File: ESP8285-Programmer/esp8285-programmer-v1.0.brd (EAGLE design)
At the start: 38.2 x 15.2 mm, 30 parts, among them J1 6p-2.54, J2 2p-2.54, J3 2p-2.54, K1 B3U-1000P, Q1 S9013, Q2 S9013, U1 CH340T-SSOP20, U2 CJA1117B-3.3-SOT89, Y1 12MHZ

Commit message: Another Rev 1.0
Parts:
- moved J1 40.7 mm to (2.54, 22.9), turned to 180 degrees
- moved F1 34.9 mm to (6.35, 16.5), turned to 0 degrees
- moved K1 34.8 mm to (6.29, 27.2), turned to 270 degrees
- moved R4 33.9 mm to (6.48, 19.4), turned to 270 degrees
- moved R5 33.5 mm to (6.48, 21.1), turned to 270 degrees
- moved R6 33.5 mm to (6.48, 22.9), turned to 270 degrees
- moved D1 30.7 mm to (37.0, 28.3), turned to 0 degrees
- moved R1 29.5 mm to (37.0, 26.5), turned to 90 degrees
- moved D4 29.2 mm to (9.59, 28.3), turned to 180 degrees
- moved R9 27.9 mm to (9.59, 26.5), turned to 270 degrees
- moved J3 25.7 mm to (11.3, 16.5), turned to 270 degrees
- moved USB 23.2 mm to (34.3, 20.3), turned to 90 degrees
- moved D2 22.9 mm to (13.1, 28.3), turned to 180 degrees
- moved Q2 22.8 mm to (11.5, 23.4), turned to 0 degrees
- moved R3 21.4 mm to (12.7, 18.9), turned to 90 degrees
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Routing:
- net N$15: track 2.64 -> 3.34 mm
- net N$14: track 2.59 -> 3.29 mm
- net N$RX: track 15.8 -> 15.1 mm
- net +3V3: track 63.0 -> 62.3 mm
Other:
- board text added: "Io0"
- board text added: "Rx"

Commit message: Hopefully final V1.0
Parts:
- moved D1 43.3 mm to (2.41, 2.16), turned to 180 degrees
- moved R1 41.2 mm to (2.41, 4.00), turned to 270 degrees
- moved J1 37.5 mm to (36.8, 7.62), turned to 0 degrees
- moved K1 35.9 mm to (33.1, 3.30), turned to 90 degrees
- moved U2 34.7 mm to (7.37, 3.05), turned to 180 degrees
- moved D4 33.0 mm to (29.8, 2.16), turned to 0 degrees
- moved USB 30.9 mm to (5.08, 10.2), turned to 270 degrees
- moved R6 30.5 mm to (32.9, 7.62), turned to 90 degrees
- moved R9 30.2 mm to (29.8, 4.00), turned to 90 degrees
- moved D2 29.3 mm to (26.2, 2.16), turned to 0 degrees
- moved C4 29.1 mm to (7.24, 7.68), turned to 0 degrees
- moved R4 28.3 mm to (32.9, 9.33), turned to 90 degrees
- moved R5 28.3 mm to (32.9, 11.0), turned to 90 degrees
- moved D3 26.8 mm to (22.7, 2.16), turned to 0 degrees
- moved F1 26.8 mm to (33.0, 14.0), turned to 180 degrees
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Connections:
- removed net N$14: J1.2, R4.2
- removed net N$15: J1.3, R5.2
- new net N$4: J1.2, R5.2
- new net N$7: J1.3, R4.2
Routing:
- net N$7: track 0.00 -> 3.36 mm
- net N$15: track 3.34 -> 0.00 mm
- net N$4: track 0.00 -> 3.33 mm
- net N$14: track 3.29 -> 0.00 mm
- net N$TX: track 17.9 -> 15.6 mm
- net N$RX: track 15.1 -> 15.8 mm

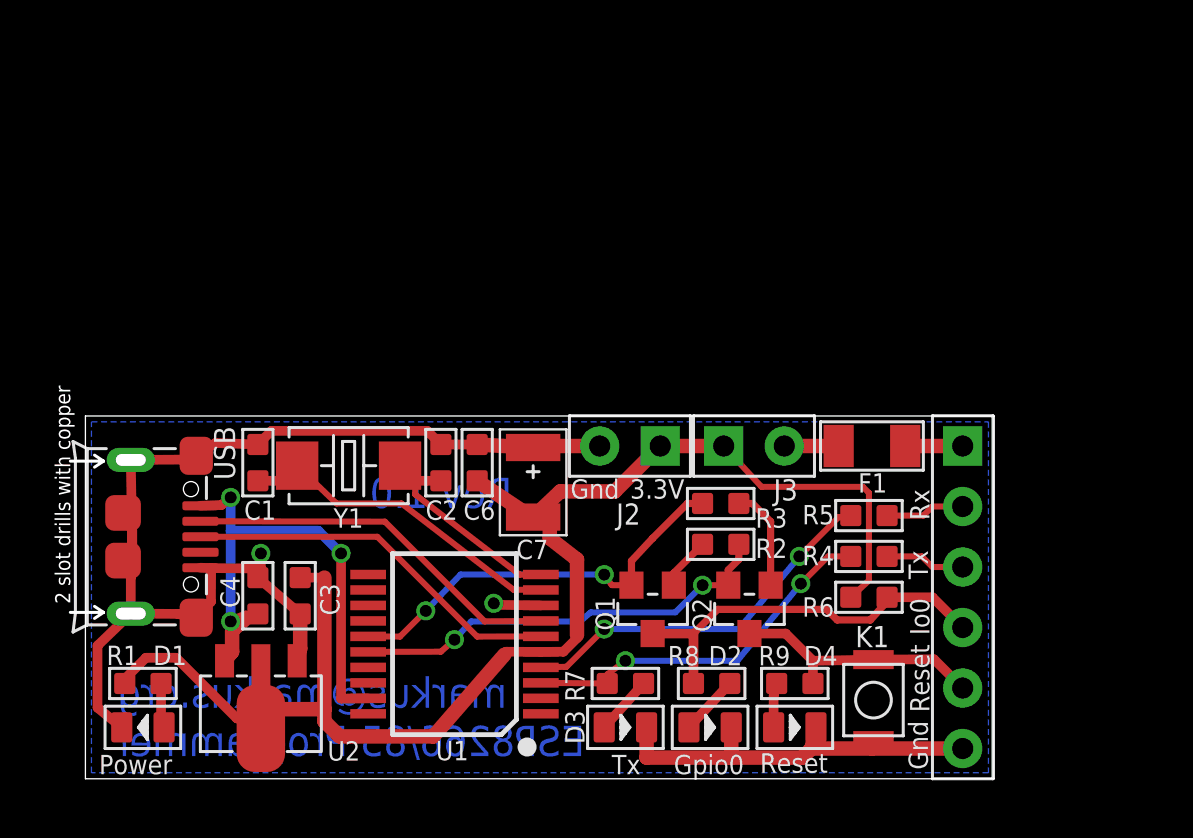
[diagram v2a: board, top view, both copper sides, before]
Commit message: Final v1.0 fixed silkscreen, added testpoint, reduced via size
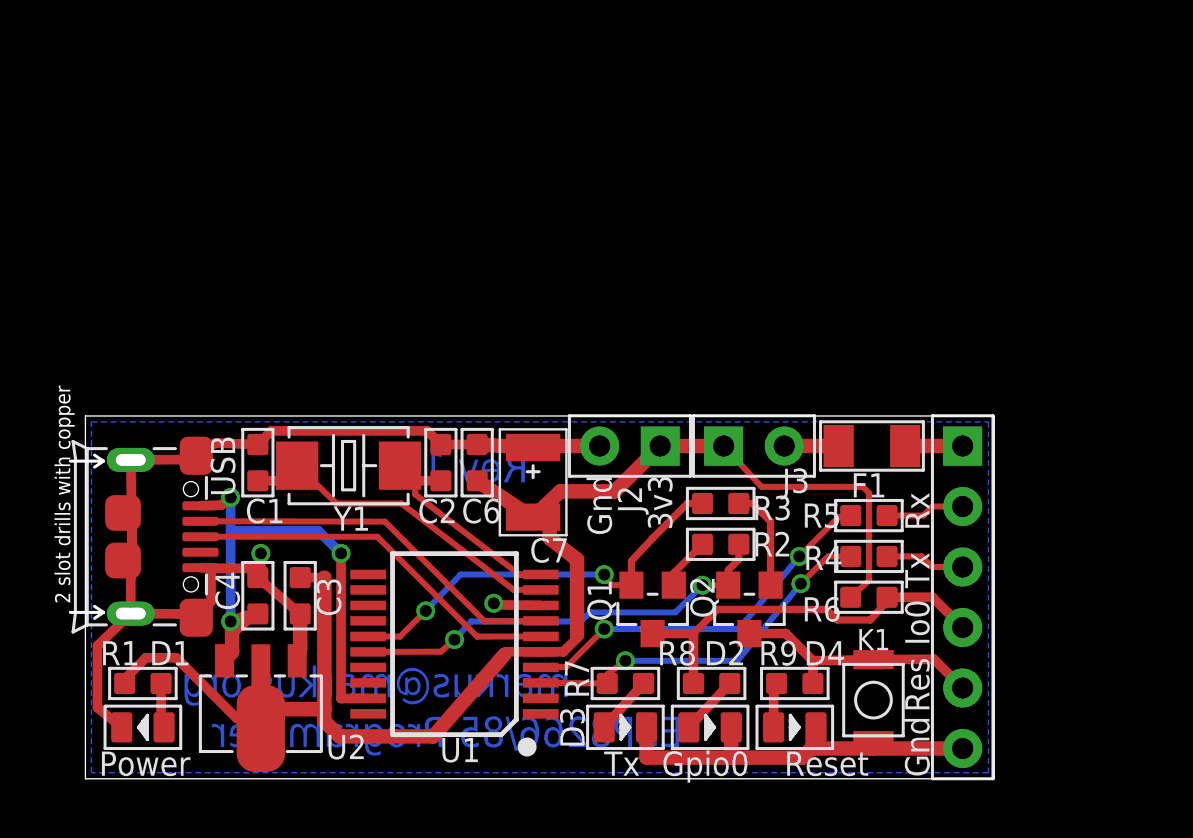
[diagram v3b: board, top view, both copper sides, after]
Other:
- board text added: "3v3"
- board text added: "Res"
- board text removed: "3.3V"
